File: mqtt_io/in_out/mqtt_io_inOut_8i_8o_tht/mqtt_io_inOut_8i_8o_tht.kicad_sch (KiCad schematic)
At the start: 109 parts, among them J1 Conn_01x04_Pin, J13 Conn_01x02, J2 Conn_01x04_Pin, K1 FINDER-40.31, K2 FINDER-40.31, K3 FINDER-40.31, K4 FINDER-40.31, K5 FINDER-40.31, K6 FINDER-40.31, K7 FINDER-40.31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

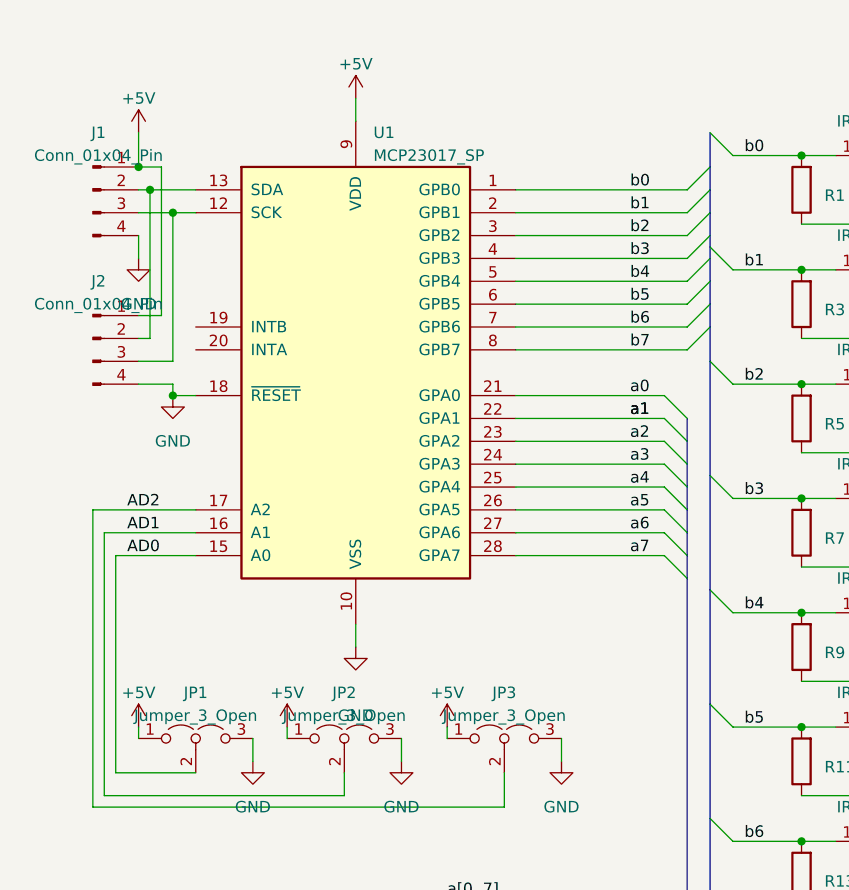
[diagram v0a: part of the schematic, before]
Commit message: Pullup für ic2 eingefügt (4k7)
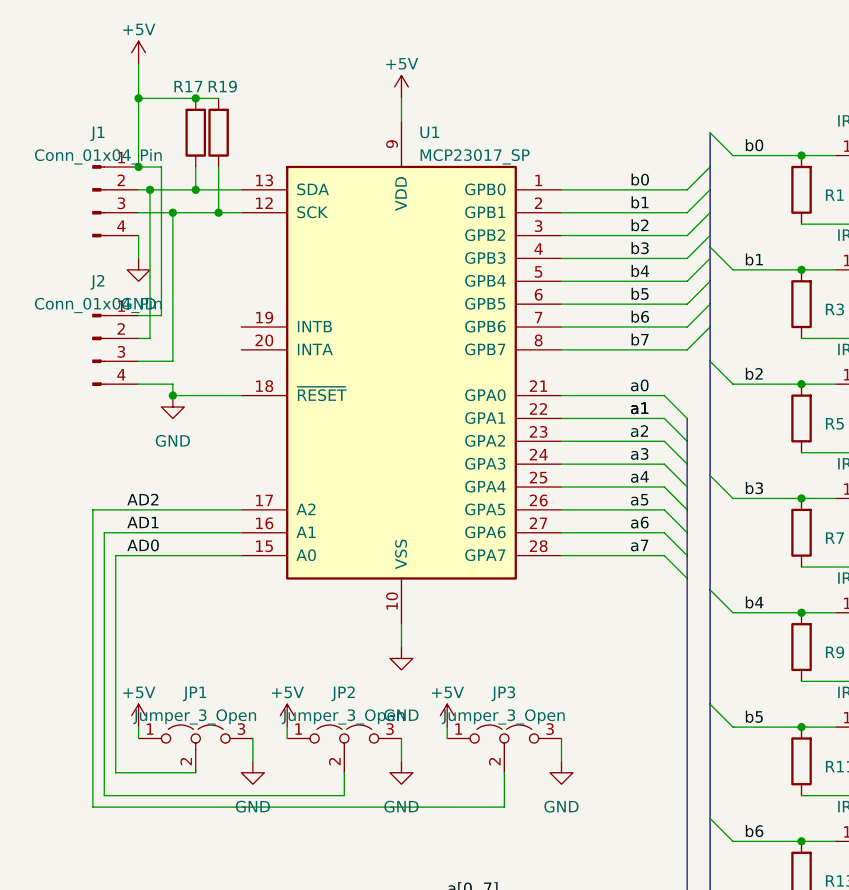
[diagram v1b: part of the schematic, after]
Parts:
- added R17, R19: 4k7, Resistor_THT:R_Axial_DIN0204_L3.6mm_D1.6mm_P7.62mm_Horizontal, symbol Device:R
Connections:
- net +5V: now also R17.2, R19.2
- net at J1.2 (Pin_2), J2.2 (Pin_2), U1.13 (SDA): now also R17.1
- net at J1.3 (Pin_3), J2.3 (Pin_3), U1.12 (SCK): now also R19.1
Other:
- moved on the sheet: U1

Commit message: neue Dateien eingefügt.
out Platine rev 2, testprogramm für pi pico
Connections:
- net GND: no longer U1.18 (~{RESET})
- net +5V renamed VDD
- net VDD: now also U1.18 (~{RESET})
